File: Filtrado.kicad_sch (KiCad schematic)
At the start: 38 parts, among them J26 Pin GND, J37 Pin GND, J38 Pin GND, J39 Pin GND, J40 Pin GND, J41 Pin GND, J42 Pin GND

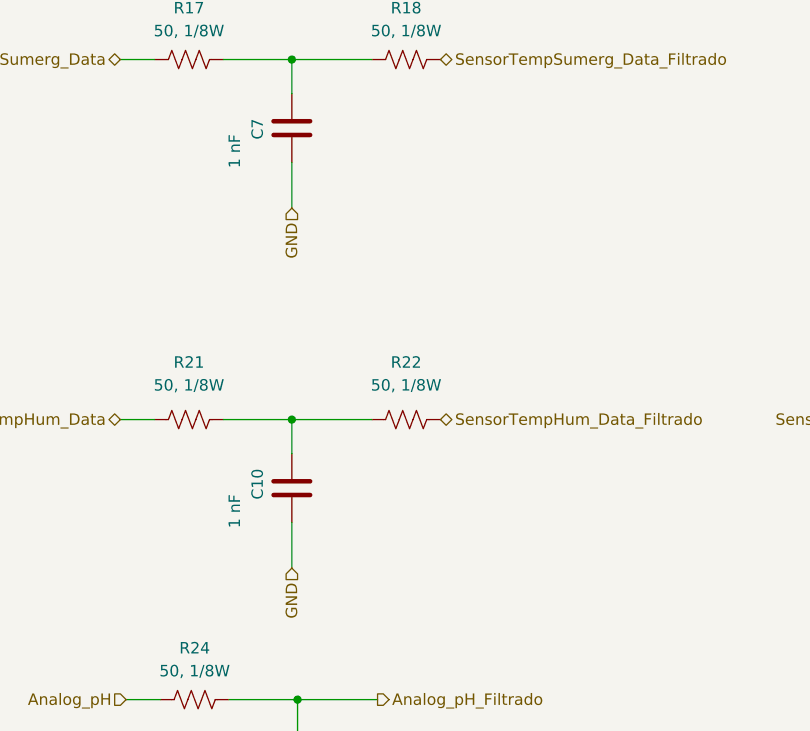
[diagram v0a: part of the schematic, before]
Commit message: Corrección de PCB.
Se agregaron algunos pin headers para conectar a GND algunos puntos. Se generaron los Gerber finales.
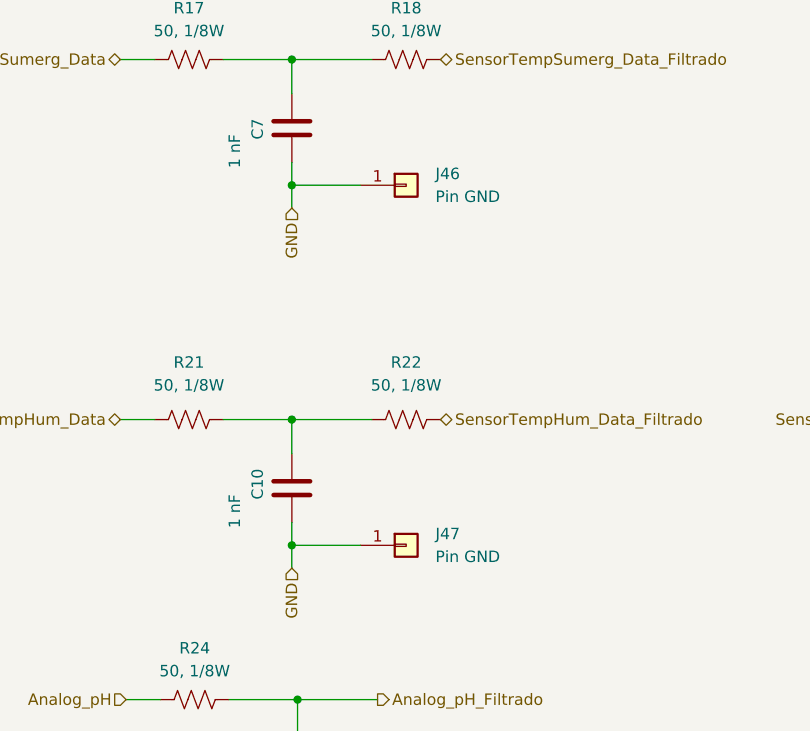
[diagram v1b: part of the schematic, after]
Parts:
- added J46, J47: Pin GND, Connector_PinHeader_2.54mm:PinHeader_1x01_P2.54mm_Vertical, symbol Connector_Generic:Conn_01x01
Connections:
- net GND: now also J46.1 (Pin_1), J47.1 (Pin_1)
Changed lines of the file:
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@@
 (kicad_sch (version 20211123) (generator eeschema)
   (paper "A4")
+  (junction (at 57.785 114.935) (diameter 0) (color 0 0 0 0)
+  )
   (junction (at 57.785 28.575) (diameter 0) (color 0 0 0 0)
   )
@@
   (junction (at 238.76 100.965) (diameter 0) (color 0 0 0 0)
   )
+  (junction (at 57.785 154.94) (diameter 0) (color 0 0 0 0)
+  )
   (junction (at 58.42 172.085) (diameter 0) (color 0 0 0 0)
   )
@@
     (stroke (width 0) (type default) (color 0 0 0 0))
   )
+  (wire (pts (xy 57.785 114.935) (xy 57.785 117.475))
+    (stroke (width 0) (type default) (color 0 0 0 0))
+  )
   (wire (pts (xy 50.165 28.575) (xy 57.785 28.575))
     (stroke (width 0) (type default) (color 0 0 0 0))
@@
     (stroke (width 0) (type default) (color 0 0 0 0))
   )
+  (wire (pts (xy 57.785 154.94) (xy 65.405 154.94))
+    (stroke (width 0) (type default) (color 0 0 0 0))
+  )
   (wire (pts (xy 58.42 172.085) (xy 67.31 172.085))
     (stroke (width 0) (type default) (color 0 0 0 0))
@@
     (stroke (width 0) (type default) (color 0 0 0 0))
   )
+  (wire (pts (xy 57.785 112.395) (xy 57.785 114.935))
+    (stroke (width 0) (type default) (color 0 0 0 0))
+  )
   (wire (pts (xy 58.42 172.085) (xy 58.42 175.895))
     (stroke (width 0) (type default) (color 0 0 0 0))
@@
     (stroke (width 0) (type default) (color 0 0 0 0))
   )
+  (wire (pts (xy 57.785 154.94) (xy 57.785 157.48))
+    (stroke (width 0) (type default) (color 0 0 0 0))
+  )
   (wire (pts (xy 238.76 64.77) (xy 238.76 68.58))
     (stroke (width 0) (type default) (color 0 0 0 0))
@@
     (stroke (width 0) (type default) (color 0 0 0 0))
   )
+  (wire (pts (xy 57.785 114.935) (xy 65.405 114.935))
+    (stroke (width 0) (type default) (color 0 0 0 0))
+  )
   (wire (pts (xy 38.735 28.575) (xy 42.545 28.575))
     (stroke (width 0) (type default) (color 0 0 0 0))
@@
     (stroke (width 0) (type default) (color 0 0 0 0))
   )
-  (wire (pts (xy 57.785 152.4) (xy 57.785 157.48))
+  (wire (pts (xy 57.785 152.4) (xy 57.785 154.94))
     (stroke (width 0) (type default) (color 0 0 0 0))
   )
@@
   )
   (wire (pts (xy 50.8 172.085) (xy 58.42 172.085))
-    (stroke (width 0) (type default) (color 0 0 0 0))
-  )
-  (wire (pts (xy 57.785 112.395) (xy 57.785 117.475))
     (stroke (width 0) (type default) (color 0 0 0 0))
   )
@@
       (effects (font (size 1.27 1.27)) hide)
     )
+    (pin "1")
+  )
+  (symbol (lib_id "Connector_Generic:Conn_01x01") (at 70.485 114.935 0) (unit 1)
+    (in_bom yes) (on_board yes) (fields_autoplaced)
+    (property "Reference" "J46" (id 0) (at 73.7362 113.6649 0)
+      (effects (font (size 1.27 1.27)) (justify left))
+    )
+    (property "Value" "Pin GND" (id 1) (at 73.7362 116.2049 0)
+      (effects (font (size 1.27 1.27)) (justify left))
+    )
+    (property "Footprint" "Connector_PinHeader_2.54mm:PinHeader_1x01_P2.54mm_Vertical" (id 2) (at 70.485 114.935 0)
+      (effects (font (size 1.27 1.27)) hide)
+    )
+    (property "Datasheet" "~" (id 3) (at 70.485 114.935 0)
+      (effects (font (size 1.27 1.27)) hide)
+    )
+    (pin "1")
+  )
+  (symbol (lib_id "Connector_Generic:Conn_01x01") (at 70.485 154.94 0) (unit 1)
+    (in_bom yes) (on_board yes) (fields_autoplaced)
+    (property "Reference" "J47" (id 0) (at 73.7362 153.6699 0)
+      (effects (font (size 1.27 1.27)) (justify left))
+    )
+    (property "Value" "Pin GND" (id 1) (at 73.7362 156.2099 0)
+      (effects (font (size 1.27 1.27)) (justify left))
+    )
+    (property "Footprint" "Connector_PinHeader_2.54mm:PinHeader_1x01_P2.54mm_Vertical" (id 2) (at 70.485 154.94 0)
+      (effects (font (size 1.27 1.27)) hide)
+    )
+    (property "Datasheet" "~" (id 3) (at 70.485 154.94 0)
+      (effects (font (size 1.27 1.27)) hide)
+    )
